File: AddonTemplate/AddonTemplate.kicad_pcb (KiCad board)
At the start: 4 copper layers, 50 x 35 mm, 3 parts, among them J1 locked

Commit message: Turns template and sensor board into two layer boards
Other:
- copper layers 4 -> 2
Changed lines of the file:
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@@
 (kicad_pcb (version 20220331) (generator pcbnew)
   (general
-    (thickness 1.6)
+    (thickness 0.57)
   )
   (paper "A4")
   (layers
     (0 "F.Cu" mixed)
-    (1 "In1.Cu" power)
-    (2 "In2.Cu" power)
     (31 "B.Cu" mixed)
-    (32 "B.Adhes" user)
-    (33 "F.Adhes" user)
+    (32 "B.Adhes" user "B.Adhesive")
+    (33 "F.Adhes" user "F.Adhesive")
     (34 "B.Paste" user)
     (35 "F.Paste" user)
-    (36 "B.SilkS" user)
-    (37 "F.SilkS" user)
+    (36 "B.SilkS" user "B.Silkscreen")
+    (37 "F.SilkS" user "F.Silkscreen")
     (38 "B.Mask" user)
     (39 "F.Mask" user)
-    (40 "Dwgs.User" user)
-    (41 "Cmts.User" user)
-    (42 "Eco1.User" user)
-    (43 "Eco2.User" user)
+    (40 "Dwgs.User" user "User.Drawings")
+    (41 "Cmts.User" user "User.Comments")
+    (42 "Eco1.User" user "User.Eco1")
+    (43 "Eco2.User" user "User.Eco2")
     (44 "Edge.Cuts" user)
     (45 "Margin" user)
-    (46 "B.CrtYd" user)
-    (47 "F.CrtYd" user)
+    (46 "B.CrtYd" user "B.Courtyard")
+    (47 "F.CrtYd" user "F.Courtyard")
     (48 "B.Fab" user)
     (49 "F.Fab" user)
@@
       (layer "F.Cu" (type "copper") (thickness 0.035))
       (layer "dielectric 1" (type "prepreg") (thickness 0.48) (material "FR4") (epsilon_r 4.5) (loss_tangent 0.02))
-      (layer "In1.Cu" (type "copper") (thickness 0.035))
-      (layer "dielectric 2" (type "prepreg") (thickness 0.48) (material "FR4") (epsilon_r 4.5) (loss_tangent 0.02))
-      (layer "In2.Cu" (type "copper") (thickness 0.035))
-      (layer "dielectric 3" (type "core") (thickness 0.48) (material "FR4") (epsilon_r 4.5) (loss_tangent 0.02))
       (layer "B.Cu" (type "copper") (thickness 0.035))
       (layer "B.Mask" (type "Bottom Solder Mask") (thickness 0.01))

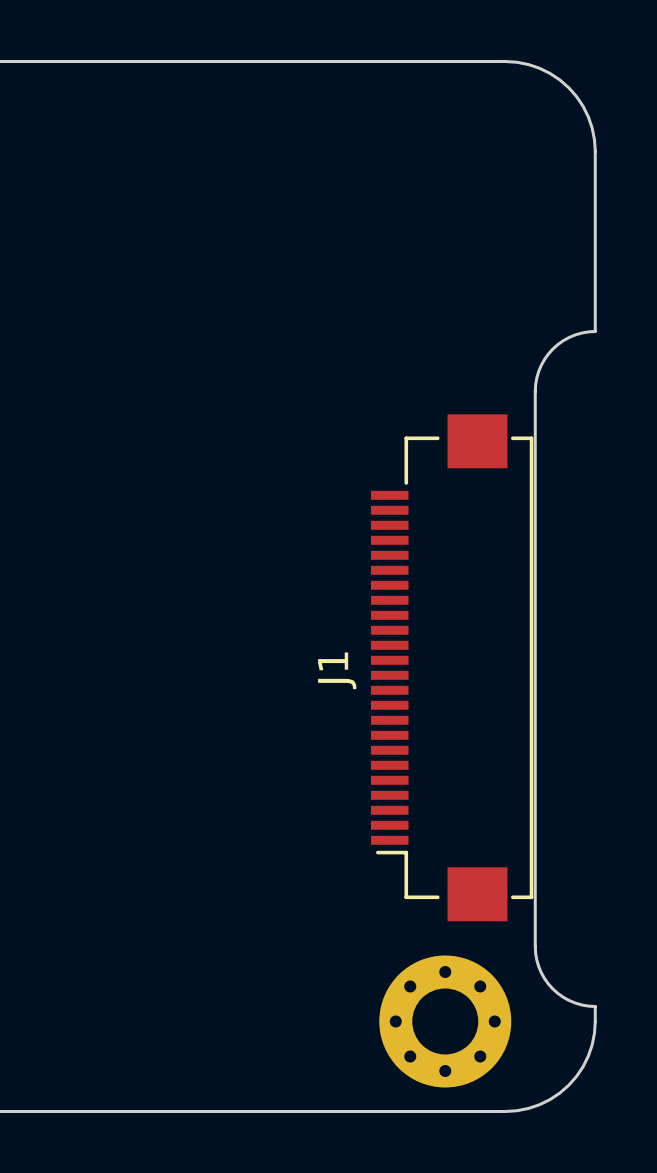
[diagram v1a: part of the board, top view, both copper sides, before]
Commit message: Adapts addon template to new version of the addon connector
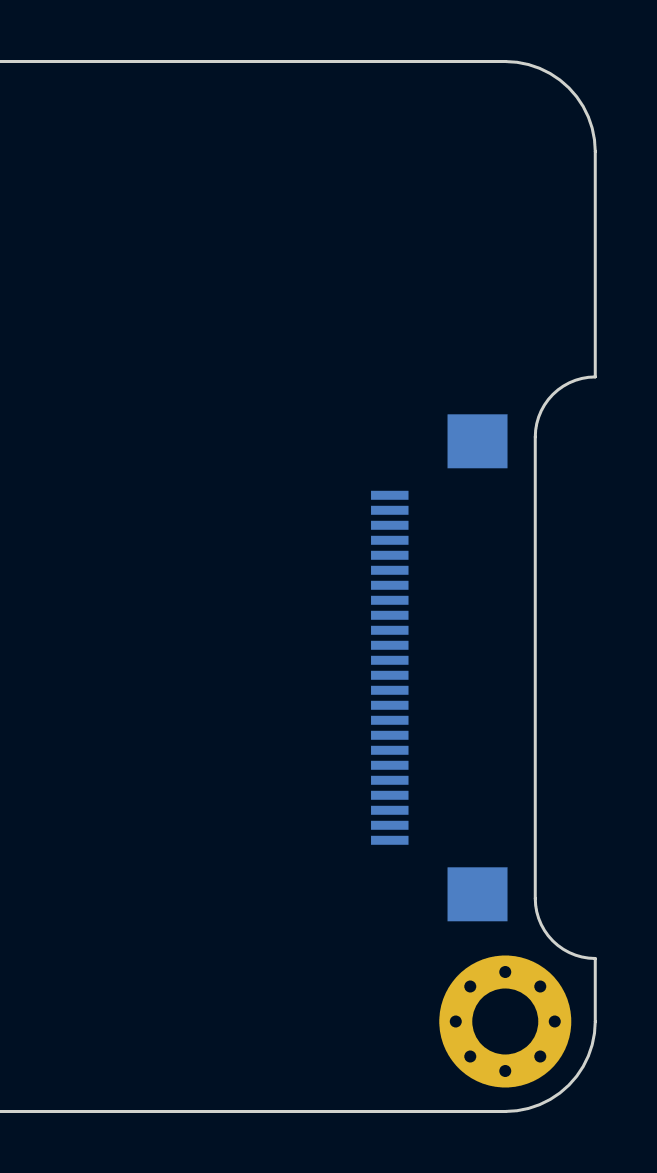
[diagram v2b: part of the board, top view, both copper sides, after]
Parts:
- J1: footprint GameOver:TXGA_FFC05036-24SBD113W5M_1x24_P0.50mm_Horizontal -> GameOver:Addon_conn_TXGA_FFC05036-24SBD113W5M_1x24_P0.50mm_Horizontal; moved to B.Cu
- moved H2 2.00 mm to (167.0, 112.0)
- turned J1 to -90 degrees
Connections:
- H1 pad 1: unconnected-(H1-Pad1) -> GND
- H2 pad 1: unconnected-(H2-Pad1) -> GND
- J1 pad 13: 3v3 -> +3V3
- J1 pad 18: GND -> unconnected-(J1-IO25)
- J1 pad 2: 3v3 -> +3V3
- J1 pad 24: 3v3 -> +3V3
- J1 pad 7: GND -> unconnected-(J1-IO5)
- J1 pad 8: 3v3 -> unconnected-(J1-IO18)
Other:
- outline, holes or cut-outs redrawn

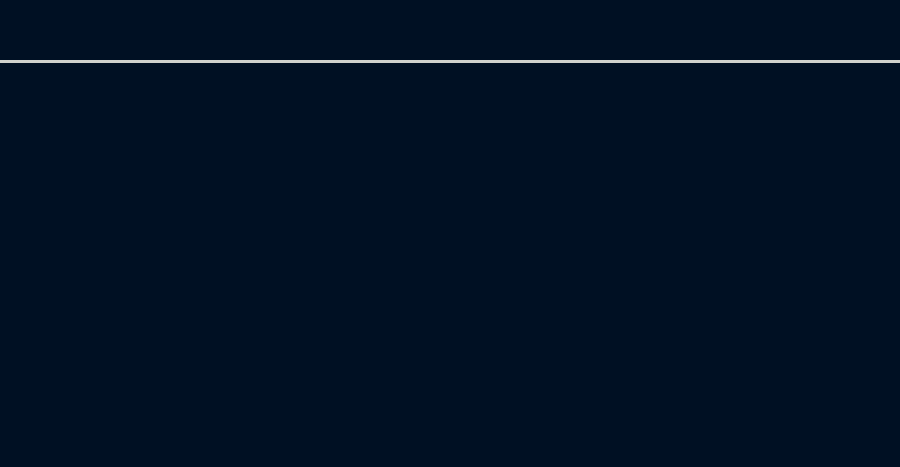
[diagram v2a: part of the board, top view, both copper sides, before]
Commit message: Updates all add-on boards with fix introduced in 692041
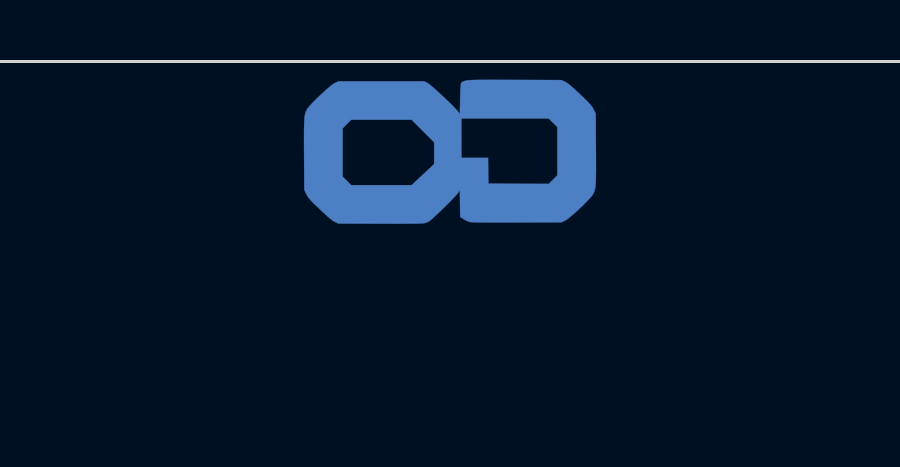
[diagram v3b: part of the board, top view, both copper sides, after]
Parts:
- added LOGO1: GameOver_logo, GameOver:logo_fcu, B.Cu at (145.0, 83.0)
